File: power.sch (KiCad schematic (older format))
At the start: 57 parts, among them J11 Conn_02x05_Odd_Even, J2 Barrel_Jack_Switch, J4 Screw_Terminal_01x12, U11 LT3471, U12 LP38693MP-1.8, U13 LP38693MP-2.5, U14 LP38692MP-5.0, U17 LM2937xMP, U19 MAX6070BAUT21+T, U21 MC79M15_TO252, U5 LP38693MP-3.3

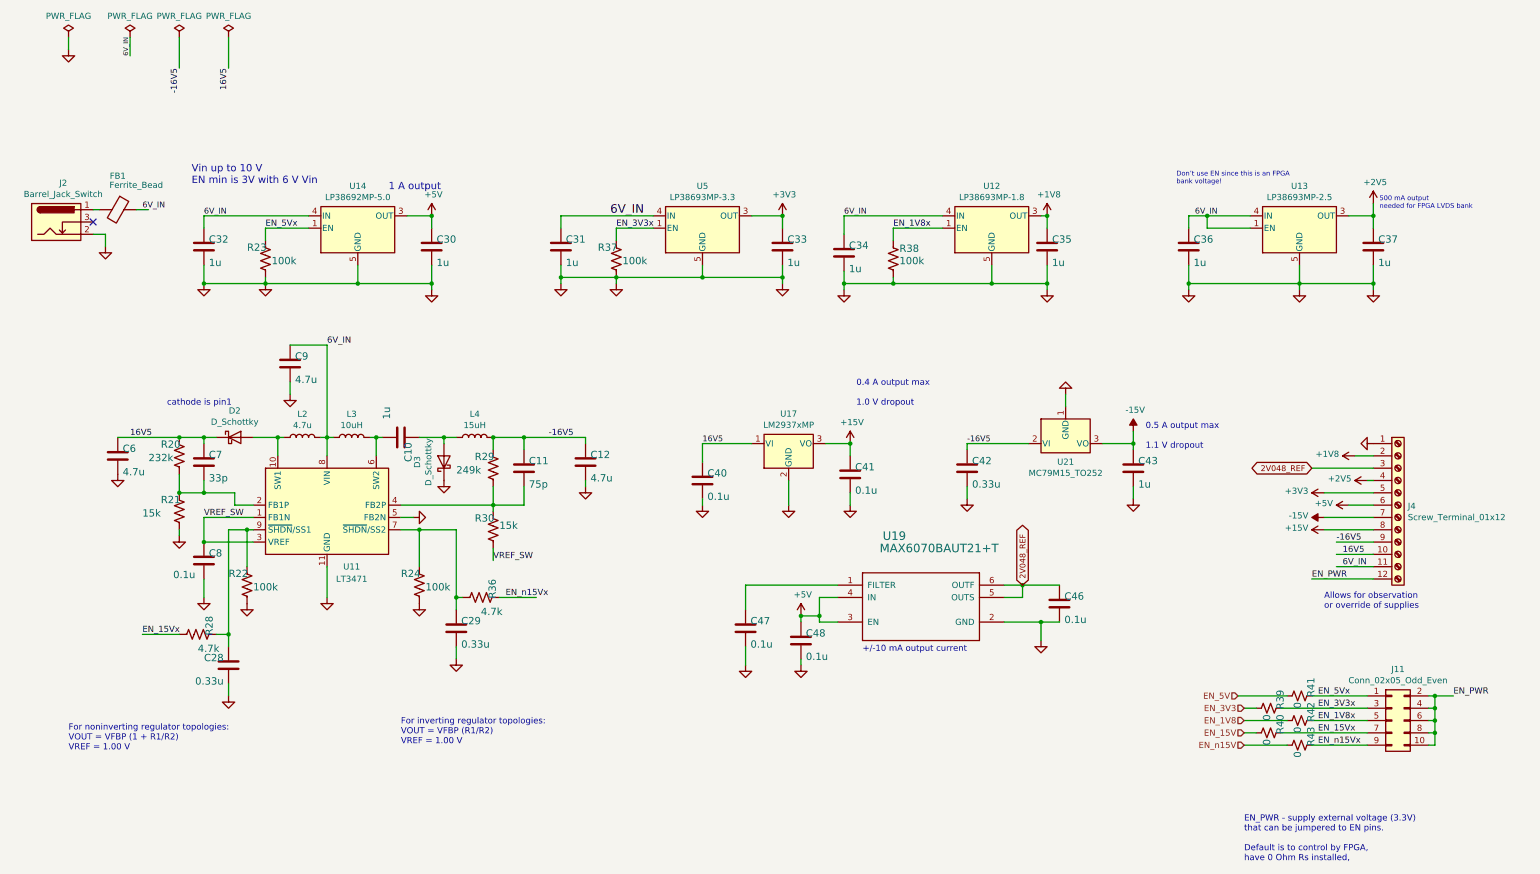
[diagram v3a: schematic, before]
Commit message: updates of DAC part placement
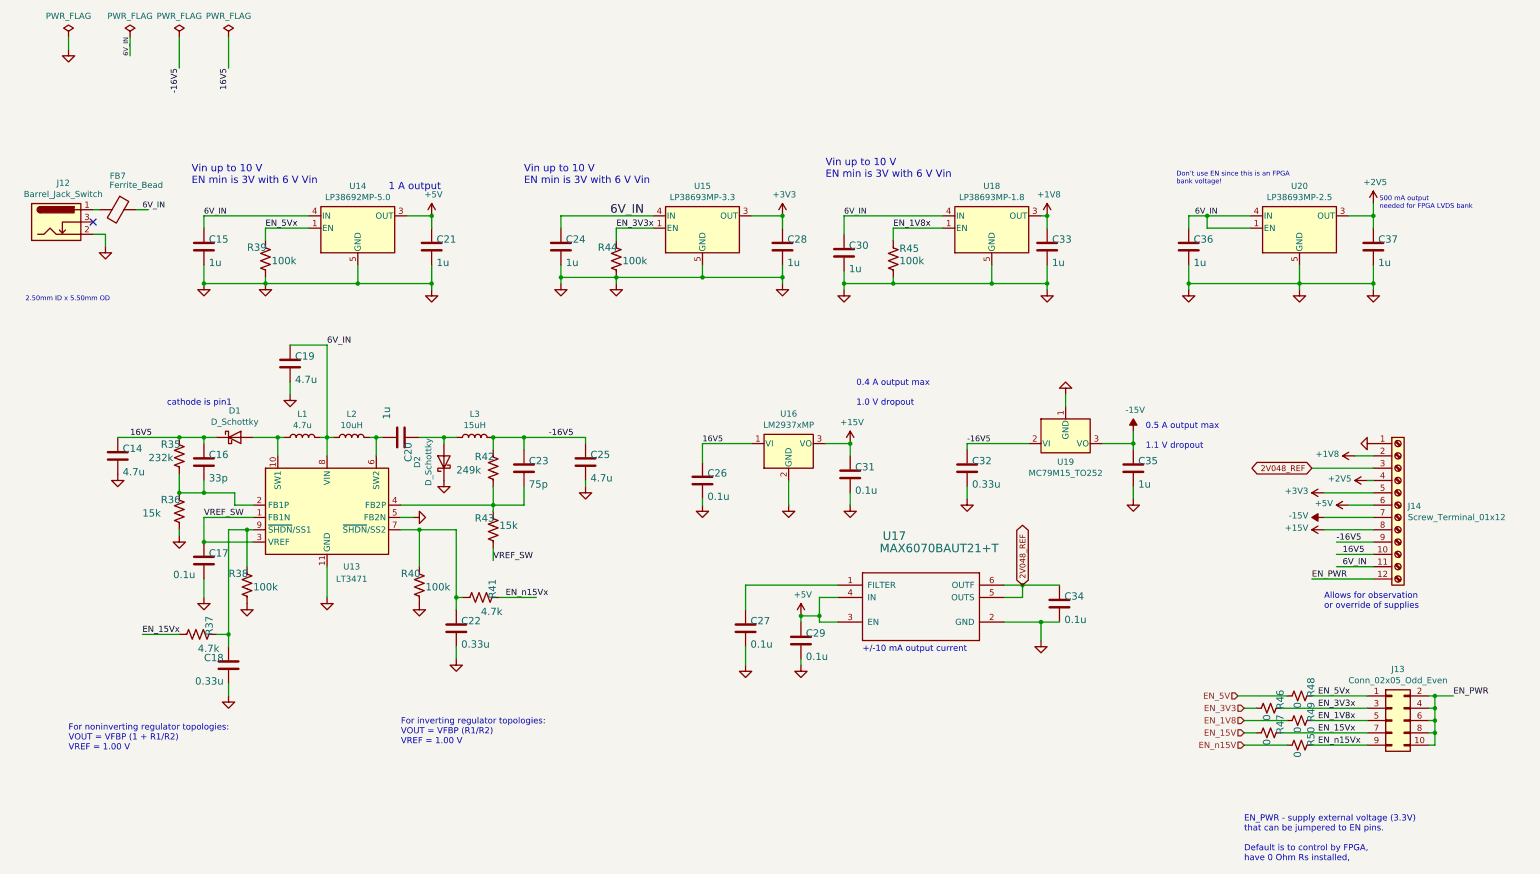
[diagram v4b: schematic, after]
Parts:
- FB7: renamed from FB1; Current Rating (none) -> 6 A; Manf# BLM31PG500SN1L -> 742792117
- J12: renamed from J2; footprint covg-kicad:CUI_PJ-002B -> covg-kicad:CUI_PJ-002BH; Manf# PJ-002B -> PJ-002BH
- renumbered C6 to C14, C32 to C15, C7 to C16, C8 to C17, C28 to C18, C9 to C19, C10 to C20, C30 to C21, C29 to C22, C11 to C23, C31 to C24, C12 to C25, C40 to C26, C47 to C27, C33 to C28, C48 to C29, C34 to C30, C41 to C31, C42 to C32, C35 to C33, C46 to C34, C43 to C35, D2 to D1, D3 to D2, J11 to J13, J4 to J14, L2 to L1, L3 to L2, L4 to L3, R20 to R35, R21 to R36, R28 to R37, R22 to R38, R23 to R39, R24 to R40, R36 to R41, R29 to R42, R30 to R43, R37 to R44, R38 to R45, R39 to R46, R40 to R47, R41 to R48, R42 to R49, R43 to R50, U11 to U13, U5 to U15, U17 to U16, U19 to U17, U12 to U18, U21 to U19, U13 to U20
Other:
- note added: "2.50mm ID x 5.50mm OD\n 5 A max\n\nCould increase input to 7 V, \n possible issues with Enables beyond that."

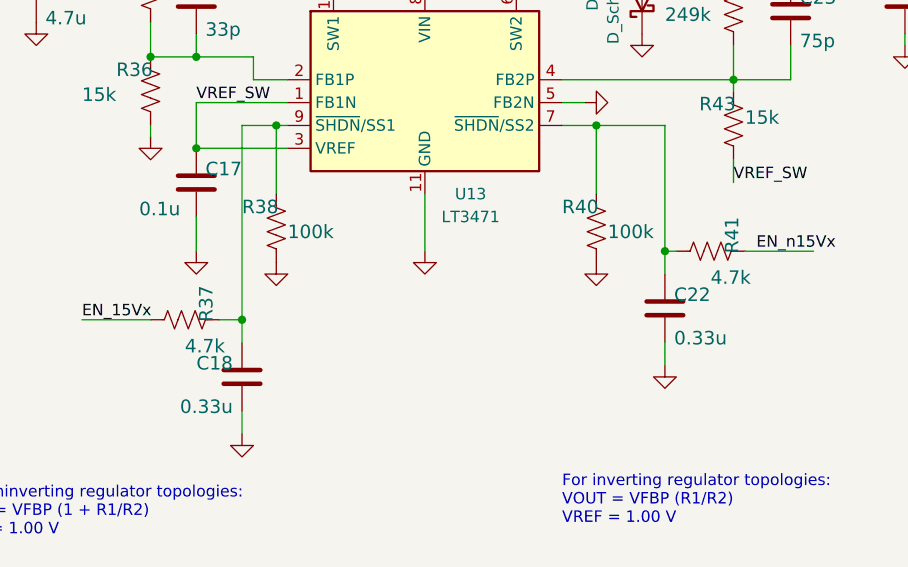
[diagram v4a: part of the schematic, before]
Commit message: updated component placement
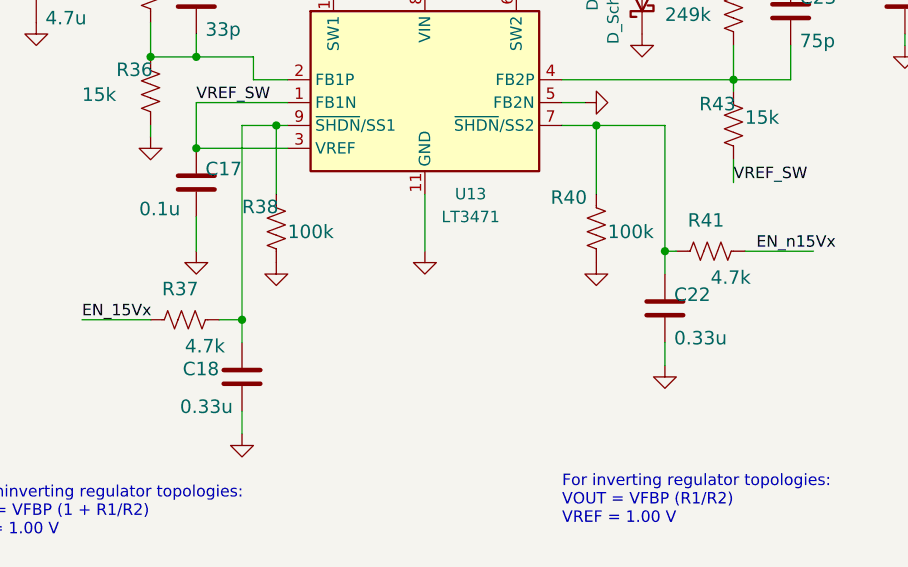
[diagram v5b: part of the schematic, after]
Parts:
- C14, C19, C25: Manf# JMK107BJ475MAHT -> TMK107BBJ475MA-T; voltage 6.3V -> 25V
- C20: Manf# CL10B105KO8NNNC -> GMK107BJ105KA-T; voltage 16V -> 35V
- D1: footprint Diode_SMD:D_Powermite2_AK -> Diode_SMD:D_Powermite_AK
- D2: footprint Diode_SMD:D_Powermite2_AK -> Diode_SMD:D_Powermite_AK; Manf# B0540W -> MBRM120LT3G
- U13: footprint Package_DFN_QFN:DFN-8-1EP_3x3mm_P0.5mm_EP1.66x2.38mm -> covg-kicad:DFN-10-1EP_3x3mm_P0.5mm_EP1.65x2.38mm
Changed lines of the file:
@@
-$EndComp
-$Comp
-L Device:R_US R42
-U 1 1 60BC667F
-P 4350 4350
-F 0 "R42" H 4200 4409 59  0000 L BNN
-F 1 "249k" H 4050 4300 59  0000 L BNN
-F 2 "Resistor_SMD:R_0603_1608Metric" H 4350 4350 50  0001 C CNN
-F 3 "" H 4350 4350 50  0001 C CNN
-F 4 "RC0603FR-07249KL" H 4200 4509 50  0001 C CNN "Manf#"
-F 5 "1%" H 4200 4509 50  0001 C CNN "Tolerance"
-	1    4350 4350
-	1    0    0    -1
 $EndComp
 $Comp
@@
 F 2 "Capacitor_SMD:C_0603_1608Metric" H 2700 3500 50  0001 C CNN
 F 3 "" H 2700 3500 50  0001 C CNN
-F 4 "JMK107BJ475MAHT" H 2740 3625 50  0001 C CNN "Manf#"
+F 4 "TMK107BBJ475MA-T" H 2740 3625 50  0001 C CNN "Manf#"
 F 5 "20%" H 2740 3625 50  0001 C CNN "Tolerance"
-F 6 "6.3V" H 2740 3625 50  0001 C CNN "voltage"
+F 6 "25V" H 2740 3625 50  0001 C CNN "voltage"
 	1    2700 3500
 	1    0    0    -1
@@
 F 0 "U13" H 3200 4350 50  0000 C CNN
 F 1 "LT3471" H 3200 4250 50  0000 C CNN
-F 2 "Package_DFN_QFN:DFN-8-1EP_3x3mm_P0.5mm_EP1.66x2.38mm" H 3000 4350 50  0001 C CNN
+F 2 "covg-kicad:DFN-10-1EP_3x3mm_P0.5mm_EP1.65x2.38mm" H 3000 4350 50  0001 C CNN
 F 3 "" H 3000 4700 50  0001 C CNN
 F 4 "LT3471EDD#PBF" H 3200 4450 50  0001 C CNN "Manf#"
@@
 F 0 "D1" H 2250 4317 50  0000 C CNN
 F 1 "D_Schottky" H 2250 4226 50  0000 C CNN
-F 2 "Diode_SMD:D_Powermite2_AK" H 2250 4100 50  0001 C CNN
+F 2 "Diode_SMD:D_Powermite_AK" H 2250 4100 50  0001 C CNN
 F 3 "~" H 2250 4100 50  0001 C CNN
 F 4 "MBRM120LT3G" H 2250 4100 50  0001 C CNN "Manf#"
@@
 F 2 "Capacitor_SMD:C_0603_1608Metric" H 1300 4250 50  0001 C CNN
 F 3 "" H 1300 4250 50  0001 C CNN
-F 4 "JMK107BJ475MAHT" H 1340 4375 50  0001 C CNN "Manf#"
+F 4 "TMK107BBJ475MA-T" H 1340 4375 50  0001 C CNN "Manf#"
 F 5 "20%" H 1340 4375 50  0001 C CNN "Tolerance"
-F 6 "6.3V" H 1340 4375 50  0001 C CNN "voltage"
+F 6 "25V" H 1340 4375 50  0001 C CNN "voltage"
 	1    1300 4250
 	1    0    0    -1
@@
 U 1 1 610C2090
 P 3750 5300
-F 0 "R40" H 3600 5359 59  0000 L BNN
+F 0 "R40" H 3550 5400 59  0000 L BNN
 F 1 "100k" H 3800 5250 59  0000 L BNN
 F 2 "Resistor_SMD:R_0603_1608Metric" H 3750 5300 50  0001 C CNN
@@
 F 2 "Capacitor_SMD:C_0603_1608Metric" H 3600 4100 50  0001 C CNN
 F 3 "" H 3600 4100 50  0001 C CNN
-F 4 "CL10B105KO8NNNC" H 3640 4225 50  0001 C CNN "Manf#"
+F 4 "GMK107BJ105KA-T" H 3640 4225 50  0001 C CNN "Manf#"
 F 5 "10%" H 3640 4225 50  0001 C CNN "Tolerance"
-F 6 "16V" H 3640 4225 50  0001 C CNN "voltage"
+F 6 "35V" H 3640 4225 50  0001 C CNN "voltage"
 	1    3600 4100
 	0    1    1    0
@@
 F 0 "D2" H 3950 4517 50  0000 C CNN
 F 1 "D_Schottky" H 3950 4426 50  0000 C CNN
-F 2 "Diode_SMD:D_Powermite2_AK" H 3950 4300 50  0001 C CNN
+F 2 "Diode_SMD:D_Powermite_AK" H 3950 4300 50  0001 C CNN
 F 3 "~" H 3950 4300 50  0001 C CNN
-F 4 "B0540W" H 3950 4300 50  0001 C CNN "Manf#"
+F 4 "MBRM120LT3G" H 3950 4300 50  0001 C CNN "Manf#"
 	1    3950 4300
-	0    -1   -1   0
-$EndComp
-$Comp
-L Device:L L3
-U 1 1 6113790E
-P 4200 4100
-F 0 "L3" V 4390 4100 50  0000 C CNN
-F 1 "15uH" V 4299 4100 50  0000 C CNN
-F 2 "covg-kicad:SRR6028-150Y" H 4200 4100 50  0001 C CNN
-F 3 "~" H 4200 4100 50  0001 C CNN
-F 4 "SRR6028-150Y‎" V 4200 4100 50  0001 C CNN "Manf#"
-	1    4200 4100
 	0    -1   -1   0
 $EndComp
@@
 F 2 "Capacitor_SMD:C_0603_1608Metric" H 5100 4300 50  0001 C CNN
 F 3 "" H 5100 4300 50  0001 C CNN
-F 4 "JMK107BJ475MAHT" H 5140 4425 50  0001 C CNN "Manf#"
+F 4 "TMK107BBJ475MA-T" H 5140 4425 50  0001 C CNN "Manf#"
 F 5 "20%" H 5140 4425 50  0001 C CNN "Tolerance"
-F 6 "6.3V" H 5140 4425 50  0001 C CNN "voltage"
+F 6 "25V" H 5140 4425 50  0001 C CNN "voltage"
 	1    5100 4300
 	1    0    0    -1
@@
 U 1 1 62A4A28C
 P 4250 5400
-F 0 "R41" H 4100 5459 59  0000 L BNN
+F 0 "R41" V 4150 5300 59  0000 L BNN
 F 1 "4.7k" V 4400 5400 59  0000 L BNN
 F 2 "Resistor_SMD:R_0603_1608Metric" H 4250 5400 50  0001 C CNN
@@
 U 1 1 62A669E7
 P 2200 5950
-F 0 "C18" H 2240 5975 59  0000 L BNN
+F 0 "C18" H 2300 5950 59  0000 L BNN
 F 1 "0.33u" H 2240 5785 59  0000 L BNN
 F 2 "Capacitor_SMD:C_0603_1608Metric" H 2200 5950 50  0001 C CNN
@@
 	3950 4100 3950 4150
 Wire Wire Line
-	3950 4100 4050 4100
-Wire Wire Line
 	5100 4500 5100 4450
 Wire Wire Line
-	4350 4200 4350 4100
-Wire Wire Line
 	3700 4750 3600 4750
 Wire Wire Line
@@
 Wire Wire Line
 	4600 4200 4600 4100
-Wire Wire Line
-	4600 4100 4350 4100
-Wire Wire Line
-	4600 4100 5100 4100
 Wire Wire Line
 	2000 4450 2000 4550
@@
 Connection ~ 1800 4100
 Connection ~ 3400 4100
-Connection ~ 3950 4100
 Connection ~ 4350 4650
-Connection ~ 4350 4100
 Connection ~ 4600 4100
 Connection ~ 2000 4550
@@
 U 1 1 60DE26F5
 P 1950 5700
-F 0 "R37" H 1800 5759 59  0000 L BNN
+F 0 "R37" V 1850 5600 59  0000 L BNN
 F 1 "4.7k" V 2100 5700 59  0000 L BNN
 F 2 "Resistor_SMD:R_0603_1608Metric" H 1950 5700 50  0001 C CNN
@@
 Text Notes 550  3000 0    39   ~ 0
 2.50mm ID x 5.50mm OD\n 5 A max\n\nCould increase input to 7 V, \n possible issues with Enables beyond that.
+Connection ~ 3950 4100
+Wire Wire Line
+	4600 4100 5100 4100
+Connection ~ 4350 4100
+Wire Wire Line
+	4600 4100 4350 4100
+Wire Wire Line
+	4350 4200 4350 4100
+Wire Wire Line
+	3950 4100 4050 4100
+$Comp
+L Device:L L3
+U 1 1 6113790E
+P 4200 4100
+F 0 "L3" V 4390 4100 50  0000 C CNN
+F 1 "15uH" V 4299 4100 50  0000 C CNN
+F 2 "covg-kicad:SRR6028-150Y" H 4200 4100 50  0001 C CNN
+F 3 "~" H 4200 4100 50  0001 C CNN
+F 4 "SRR6028-150Y‎" V 4200 4100 50  0001 C CNN "Manf#"
+	1    4200 4100
+	0    -1   -1   0
+$EndComp
+$Comp
+L Device:R_US R42
+U 1 1 60BC667F
+P 4350 4350
+F 0 "R42" H 4200 4409 59  0000 L BNN
+F 1 "249k" H 4050 4300 59  0000 L BNN
+F 2 "Resistor_SMD:R_0603_1608Metric" H 4350 4350 50  0001 C CNN
+F 3 "" H 4350 4350 50  0001 C CNN
+F 4 "RC0603FR-07249KL" H 4200 4509 50  0001 C CNN "Manf#"
+F 5 "1%" H 4200 4509 50  0001 C CNN "Tolerance"
+	1    4350 4350
+	1    0    0    -1
+$EndComp
 $EndSCHEMATC

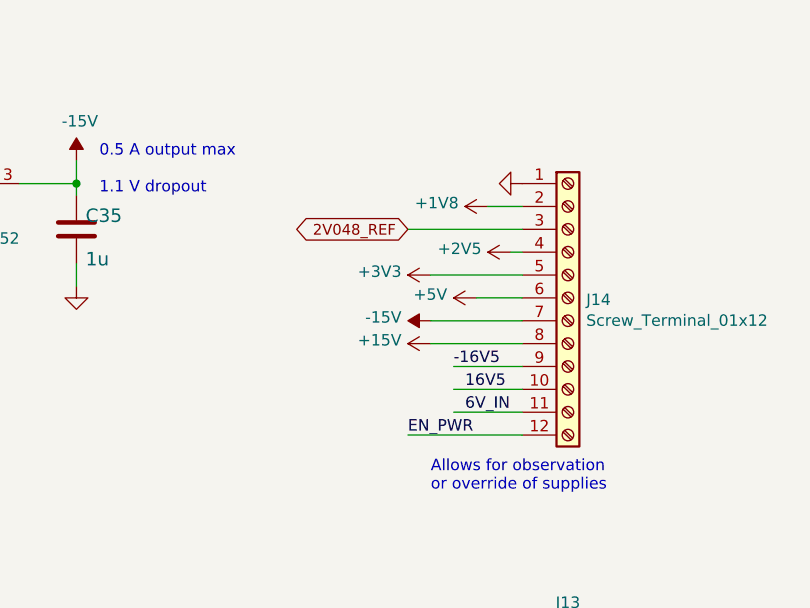
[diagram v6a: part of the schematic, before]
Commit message: finished parts placement; reconnecting pins for less spagheti
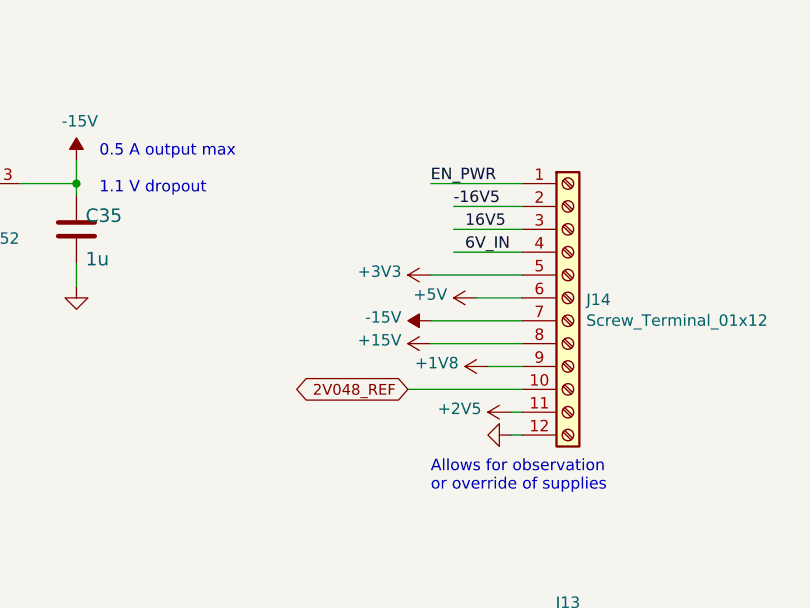
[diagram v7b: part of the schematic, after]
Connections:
- net +1V8: now also J14.9 (Pin_9); no longer J14.2 (Pin_2)
- net +2V5: now also J14.11 (Pin_11); no longer J14.4 (Pin_4)
- net -16V5: now also J14.2 (Pin_2); no longer J14.9 (Pin_9)
- net 16V5: now also J14.3 (Pin_3); no longer J14.10 (Pin_10)
- net 2V048_REF: now also J14.10 (Pin_10); no longer J14.3 (Pin_3)
- net 6V_IN: now also J14.4 (Pin_4); no longer J14.11 (Pin_11)
- net EN_PWR: now also J14.1 (Pin_1); no longer J14.12 (Pin_12)
- net GND: now also J14.12 (Pin_12); no longer J14.1 (Pin_1)
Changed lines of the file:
@@
 L power:+1V8 #PWR075
 U 1 1 61303020
-P 11350 4250
-F 0 "#PWR075" H 11350 4100 50  0001 C CNN
-F 1 "+1V8" V 11365 4378 50  0000 L CNN
-F 2 "" H 11350 4250 50  0001 C CNN
-F 3 "" H 11350 4250 50  0001 C CNN
-	1    11350 4250
+P 11350 4950
+F 0 "#PWR075" H 11350 4800 50  0001 C CNN
+F 1 "+1V8" V 11365 5078 50  0000 L CNN
+F 2 "" H 11350 4950 50  0001 C CNN
+F 3 "" H 11350 4950 50  0001 C CNN
+	1    11350 4950
 	0    -1   -1   0
 $EndComp
@@
 L power:+2V5 #PWR076
 U 1 1 60C2A239
-P 11450 4450
-F 0 "#PWR076" H 11450 4300 50  0001 C CNN
-F 1 "+2V5" V 11465 4578 50  0000 L CNN
-F 2 "" H 11450 4450 50  0001 C CNN
-F 3 "" H 11450 4450 50  0001 C CNN
-	1    11450 4450
+P 11450 5150
+F 0 "#PWR076" H 11450 5000 50  0001 C CNN
+F 1 "+2V5" V 11465 5278 50  0000 L CNN
+F 2 "" H 11450 5150 50  0001 C CNN
+F 3 "" H 11450 5150 50  0001 C CNN
+	1    11450 5150
 	0    -1   -1   0
 $EndComp
@@
 	1    2200 6200
 	-1   0    0    -1
-$EndComp
-$Comp
-L power:GND #GND057
-U 1 1 62AC7523
-P 11500 4150
-F 0 "#GND057" H 11500 4150 50  0001 C CNN
-F 1 "GND" H 11400 4050 59  0001 L BNN
-F 2 "" H 11500 4150 50  0001 C CNN
-F 3 "" H 11500 4150 50  0001 C CNN
-	1    11500 4150
-	0    1    1    0
 $EndComp
 $Comp
@@
 Text Notes 7300 3850 0    50   ~ 0
 0.4 A output max\n\n1.0 V dropout
-Text Label 11200 4950 0    50   ~ 0
+Text Label 11200 4250 0    50   ~ 0
 -16V5
-Text Label 11250 5050 0    50   ~ 0
+Text Label 11250 4350 0    50   ~ 0
 16V5
-Text Label 11250 5150 0    50   ~ 0
+Text Label 11250 4450 0    50   ~ 0
 6V_IN
 Text Notes 11100 5500 0    50   ~ 0
@@
 Text HLabel 10450 6500 0    50   Input ~ 0
 EN_15V
-Text GLabel 11000 4350 0    47   BiDi ~ 0
+Text GLabel 11000 5050 0    47   BiDi ~ 0
 2V048_REF
 Text Label 1500 2250 0    47   ~ 0
@@
 Text Notes 9900 2050 0    39   ~ 0
 Don’t use EN since this is an FPGA\nbank voltage!
-Text Label 11000 5250 0    50   ~ 0
+Text Label 11100 4150 0    50   ~ 0
 EN_PWR
 Text Label 12150 6200 0    50   ~ 0
@@
 	1200 2450 1100 2450
 Wire Wire Line
-	11200 5050 11500 5050
-Wire Wire Line
-	11200 4950 11500 4950
-Wire Wire Line
-	11000 4350 11500 4350
+	11200 4350 11500 4350
+Wire Wire Line
+	11200 4250 11500 4250
+Wire Wire Line
+	11000 5050 11500 5050
 Wire Wire Line
 	7000 5400 7000 5550
@@
 	11500 4550 11100 4550
 Wire Wire Line
-	11500 4450 11450 4450
+	11500 5150 11450 5150
 Wire Wire Line
 	2000 2400 2000 2300
@@
 	6050 4650 6050 4600
 Wire Wire Line
-	11200 5150 11500 5150
+	11200 4450 11500 4450
 Wire Wire Line
 	10000 2400 10000 2300
@@
 	3600 4850 3750 4850
 Wire Wire Line
-	11350 4250 11500 4250
+	11350 4950 11500 4950
 Wire Wire Line
 	1450 2250 1550 2250
@@
 Wire Wire Line
 	10150 2300 10500 2300
-Wire Wire Line
-	11000 5250 11500 5250
 Wire Wire Line
 	12150 6200 12000 6200
@@
 	1    0    0    -1
 $EndComp
+$Comp
+L power:GND #GND?
+U 1 1 60FF305F
+P 11450 5250
+F 0 "#GND?" H 11450 5250 50  0001 C CNN
+F 1 "GND" H 11350 5150 59  0001 L BNN
+F 2 "" H 11450 5250 50  0001 C CNN
+F 3 "" H 11450 5250 50  0001 C CNN
+	1    11450 5250
+	0    1    1    0
+$EndComp
+Wire Wire Line
+	11450 5250 11500 5250
+Wire Wire Line
+	11100 4150 11500 4150
 $EndSCHEMATC
